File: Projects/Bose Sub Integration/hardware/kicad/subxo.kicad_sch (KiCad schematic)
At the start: 44 parts, among them J1 IN L, J2 IN R, J3 OUT 3.5mm, J4 PWR IN 15V, J5 POLARITY SW, J6 LEVEL POT 10k, J7 INV LED, U1 TL074, U2 LM7812

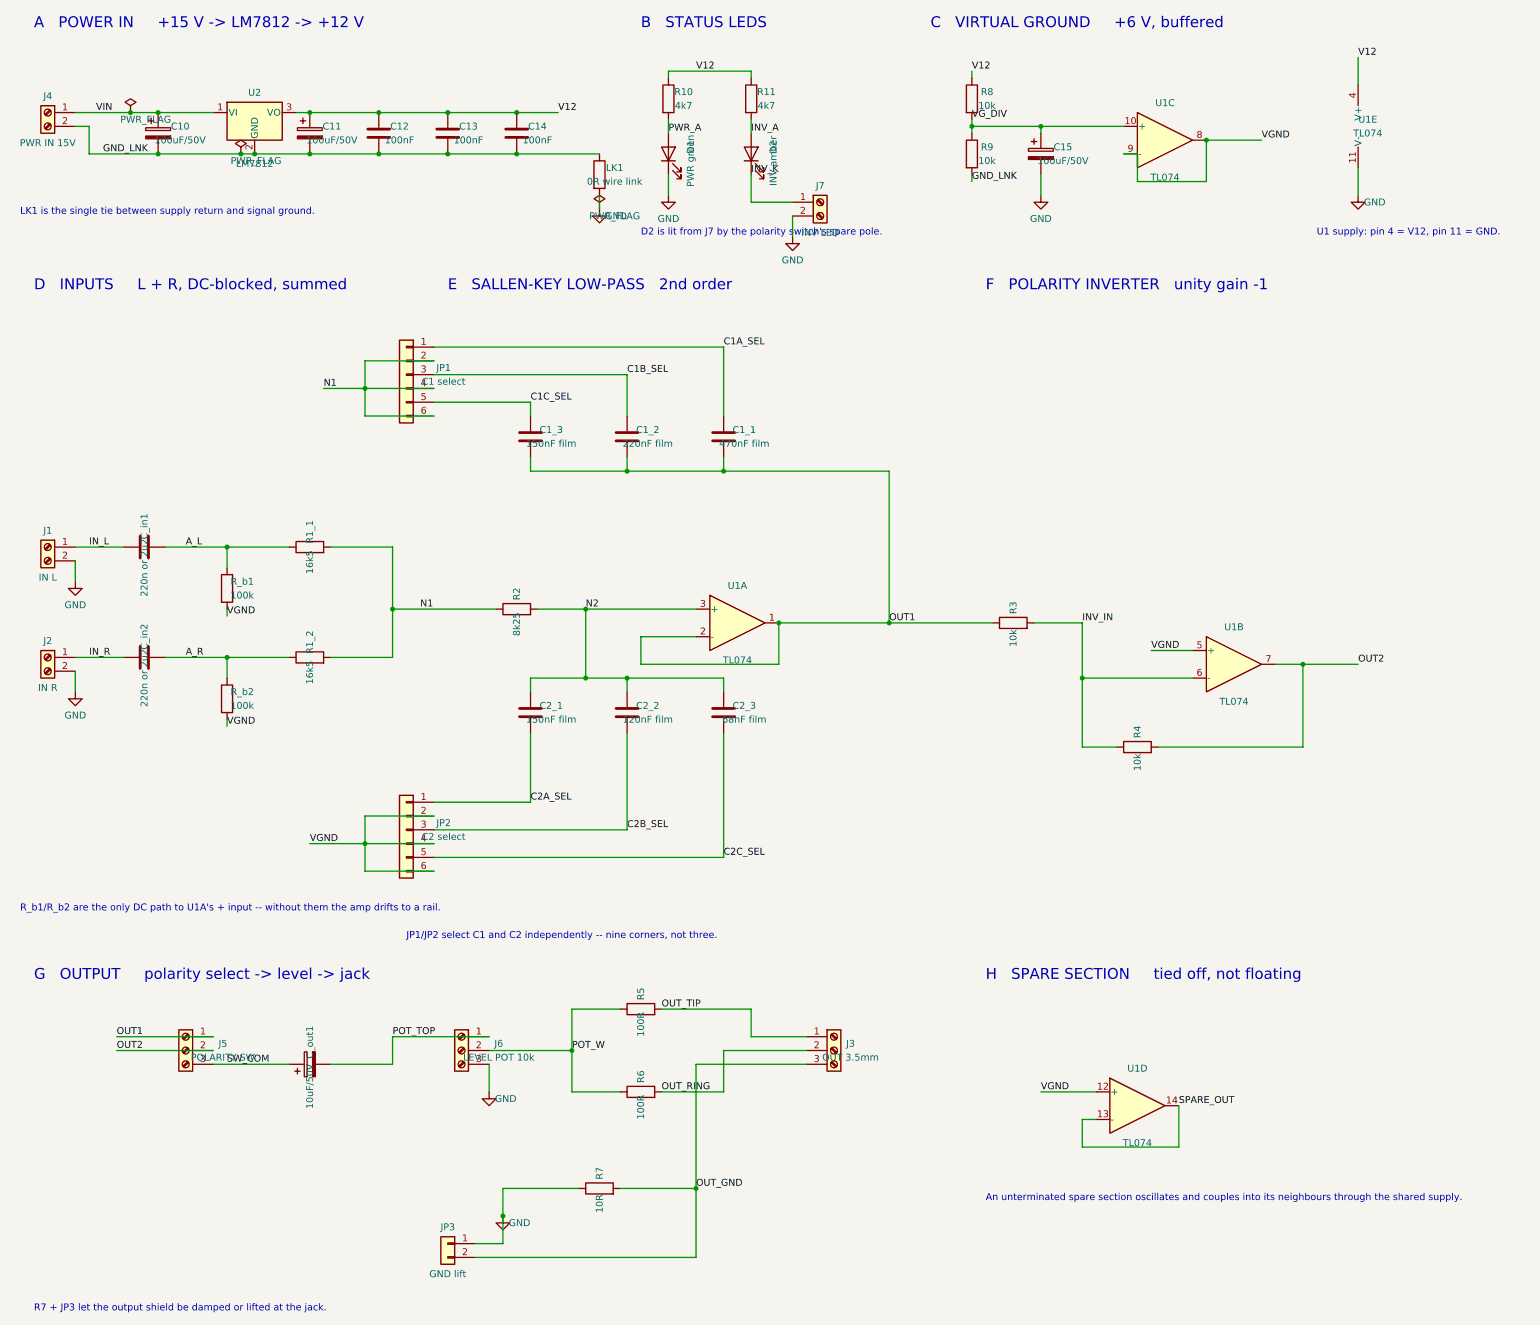
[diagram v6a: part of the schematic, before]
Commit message: Sub crossover: transplant the layout into the original sheet
Emitting the schematic from scratch kept tripping over structural conventions
that kicad-cli tolerates and Eeschema does not. Every generated file netted up
correctly under kicad-cli and rendered correctly, yet the GUI reported 23
unconnected pins, and chasing that from outside the GUI cost far more than it
was worth.

So the sheet is no longer generated. sch_retrofit.py takes the original board -
a file this KiCad demonstrably accepts - keeps its header, its uuid, its
lib_symbols and every symbol block as they are, and changes only what a redraw
actually needs to change: where each symbol sits, and the wires, junctions,
labels and notes. Power ports the layout adds are cloned from the original's
own PWR_FLAG block so even those follow the file's conventions rather than
ours. Stale symbols the new layout does not use are removed rather than
stranded at their old coordinates.

ERC now reports 9 lib_symbol_mismatch and nothing else - the same nine the
original board reports. Netlist identical at 44 parts / 31 nets / 112 nodes,
and all eleven readability checks pass: 8% stitched against 97%, 92% of pins
wired to another part against 13%.
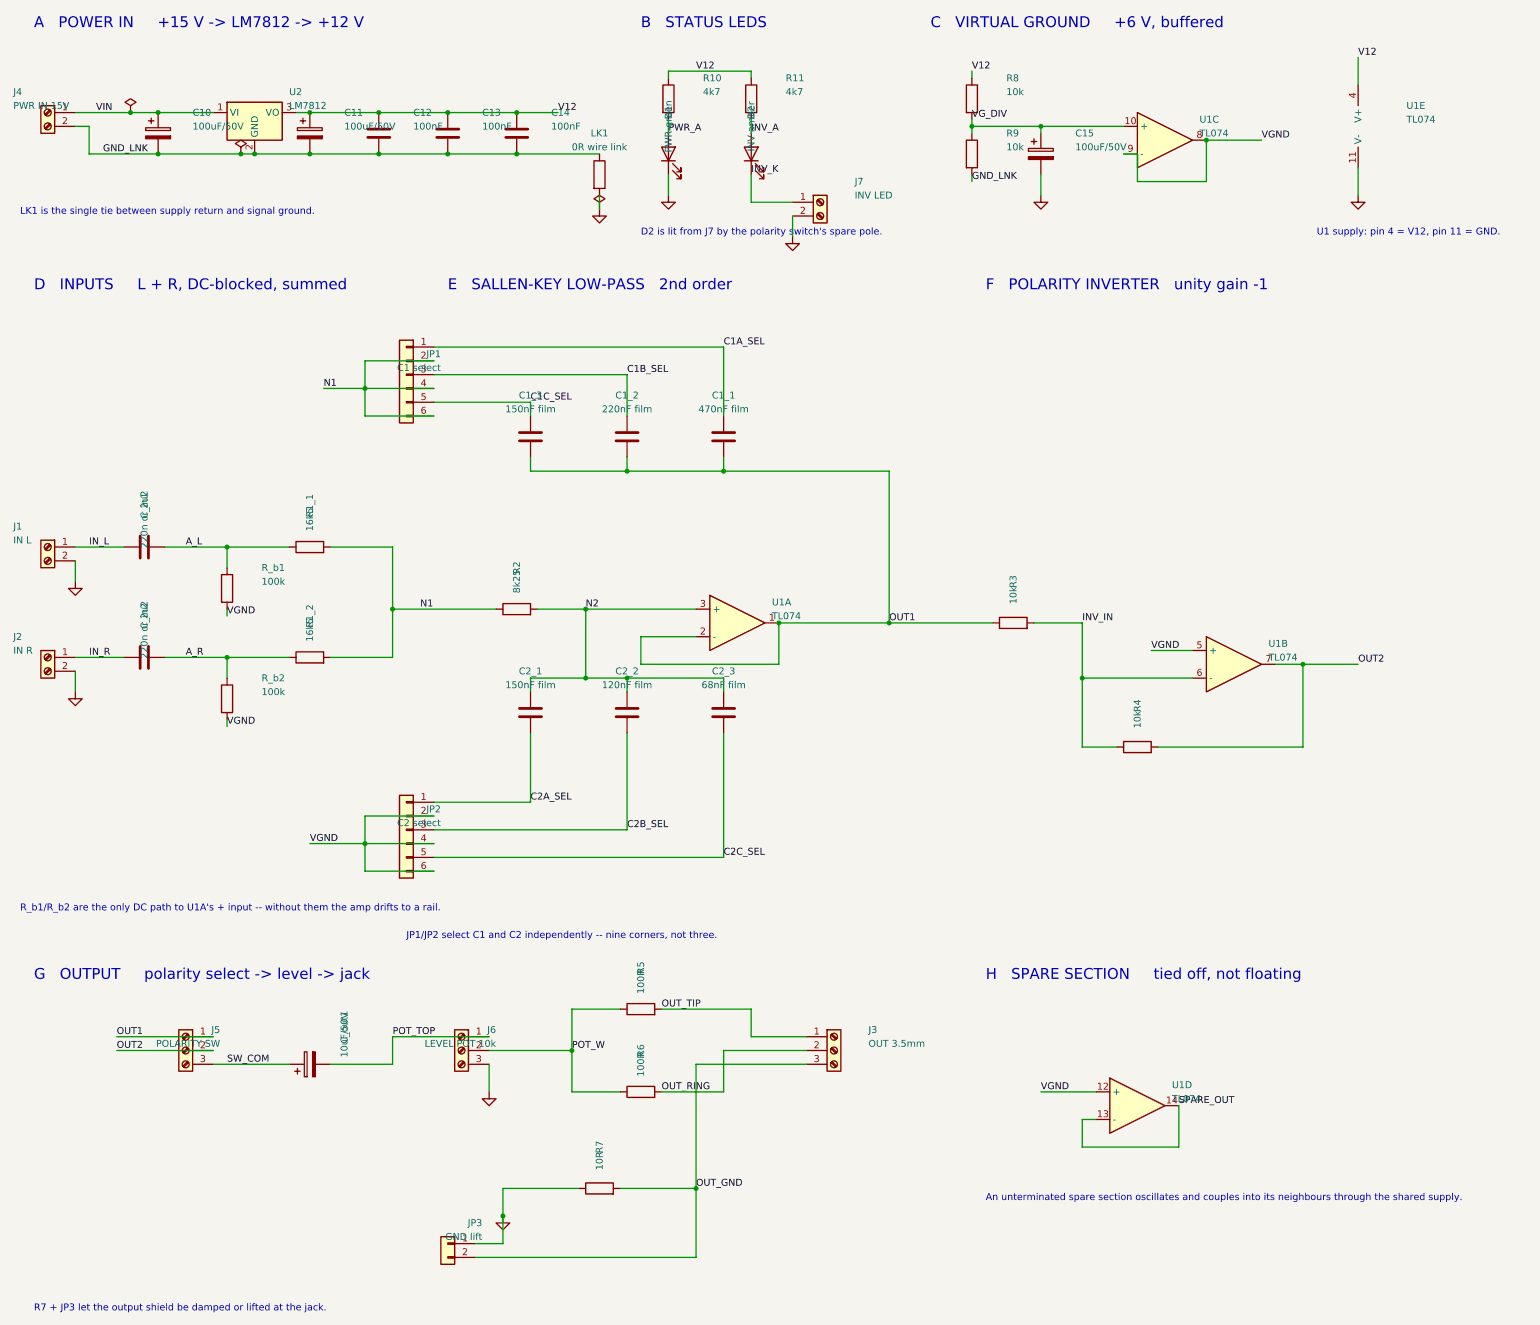
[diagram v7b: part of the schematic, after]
